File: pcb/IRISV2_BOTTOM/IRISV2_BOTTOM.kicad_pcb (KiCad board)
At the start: 4 copper layers, 50 x 50 mm, 92 parts, among them J1 Screw_Terminal_01x02, J10 Screw_Terminal_01x02, J11 Screw_Terminal_01x02, J12 Screw_Terminal_01x02, J13 Screw_Terminal_01x02, J14 Screw_Terminal_01x02, J15 Screw_Terminal_01x02, J16 Screw_Terminal_01x02, J3 Conn_01x20_MountingPin, J9 Screw_Terminal_01x02, Q1 BC846, Q10 PJA3404A, Q11 PJA3404A, Q12 PJA3404A, Q13 BC846, Q14 MCAC011P03L-TP, Q15 BC846, Q16 MCAC011P03L-TP, Q17 BC846, Q2 BC846, Q3 BC846, Q4 PJA3404A, Q5 PJA3404A, Q6 PJA3404A, Q7 BC846, Q8 BC846, Q9 BC846, U1 TPS613222ADBV, U2 INA237, U3 MP4323GDE-Z

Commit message: all main routing done, need to break out remaining gpio onto banks of mpu and ppu
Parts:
- added J4: Screw_Terminal_01x03, OSTTE030104:OSTTE030104, F.Cu at (165.7, 126.4)
- moved R43 2.23 mm to (166.8, 121.1), turned to -90 degrees
- moved Q9 1.65 mm to (170.4, 120.6)
- moved R46 1.63 mm to (167.8, 121.1)
- moved Q12 1.59 mm to (170.2, 116.8)
- moved R49 0.54 mm to (167.4, 119.6)
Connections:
- net buzzer renamed /buzzer
- net ina_scl renamed /ina_scl
- net ina_sda renamed /ina_sda
- J3 pad 13: GND -> /can_h
- J3 pad 15: GND -> /can_l
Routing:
- net /can_h: track 0.00 -> 61.6 mm, vias 0 -> 1
- net /can_l: track 0.00 -> 58.0 mm, vias 0 -> 1
- net c6_fire: track 50.8 -> 52.2 mm
- net /power_control/c6_-: track 5.80 -> 6.46 mm

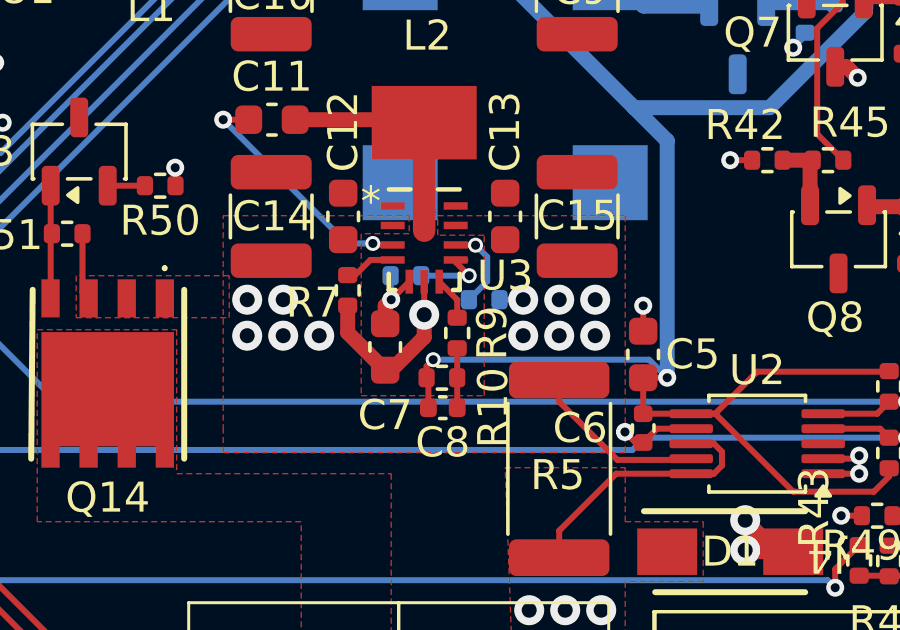
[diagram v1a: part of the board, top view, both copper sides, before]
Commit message: fixed some issues, lr2021 matching is now 0201 - todo change trace width to match pad width like ref design, see todo for rest
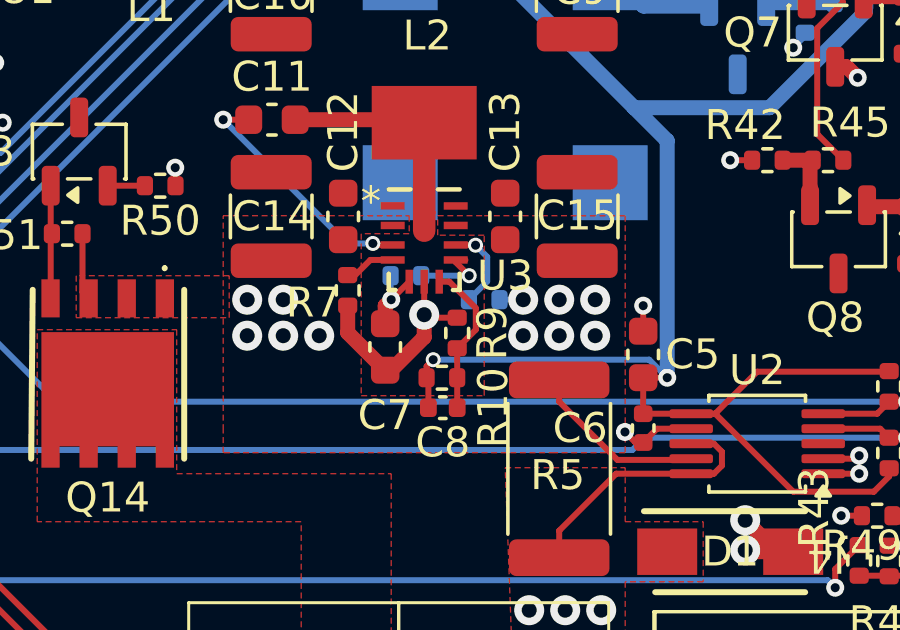
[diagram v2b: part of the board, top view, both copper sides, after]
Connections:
- C8 pad 1: Net-(C8-Pad1) -> /feedback
- R10 pad 2: Net-(C8-Pad1) -> /feedback
- R9 pad 1: /feedback -> GND
- R9 pad 2: Net-(C8-Pad1) -> /feedback
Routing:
- net /feedback: track 1.45 -> 5.16 mm
- net Net-(C8-Pad1): track 1.98 -> 0.00 mm
- net GND: track 20.3 -> 21.5 mm

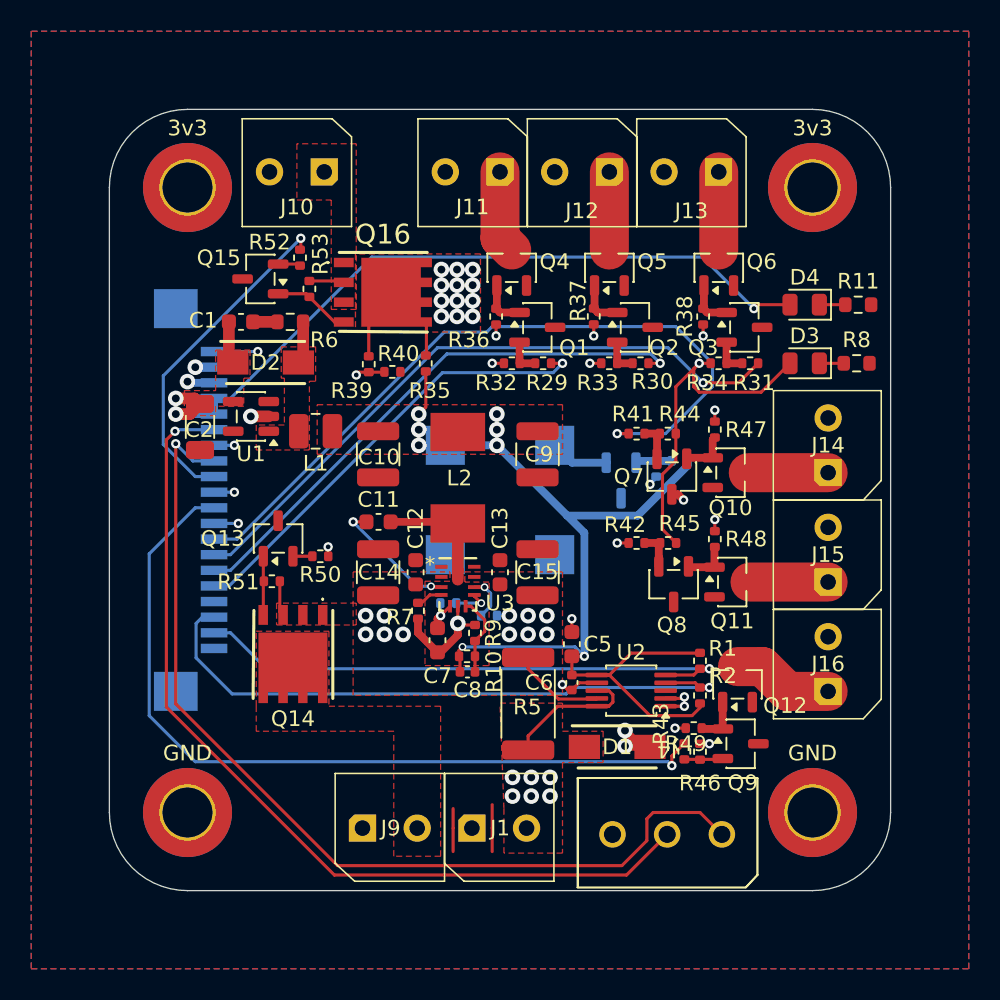
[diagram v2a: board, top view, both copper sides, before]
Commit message: removed usb, added connectors and stuff, 3d models mostly added, still need to route out gpio and servos (though connectors added)
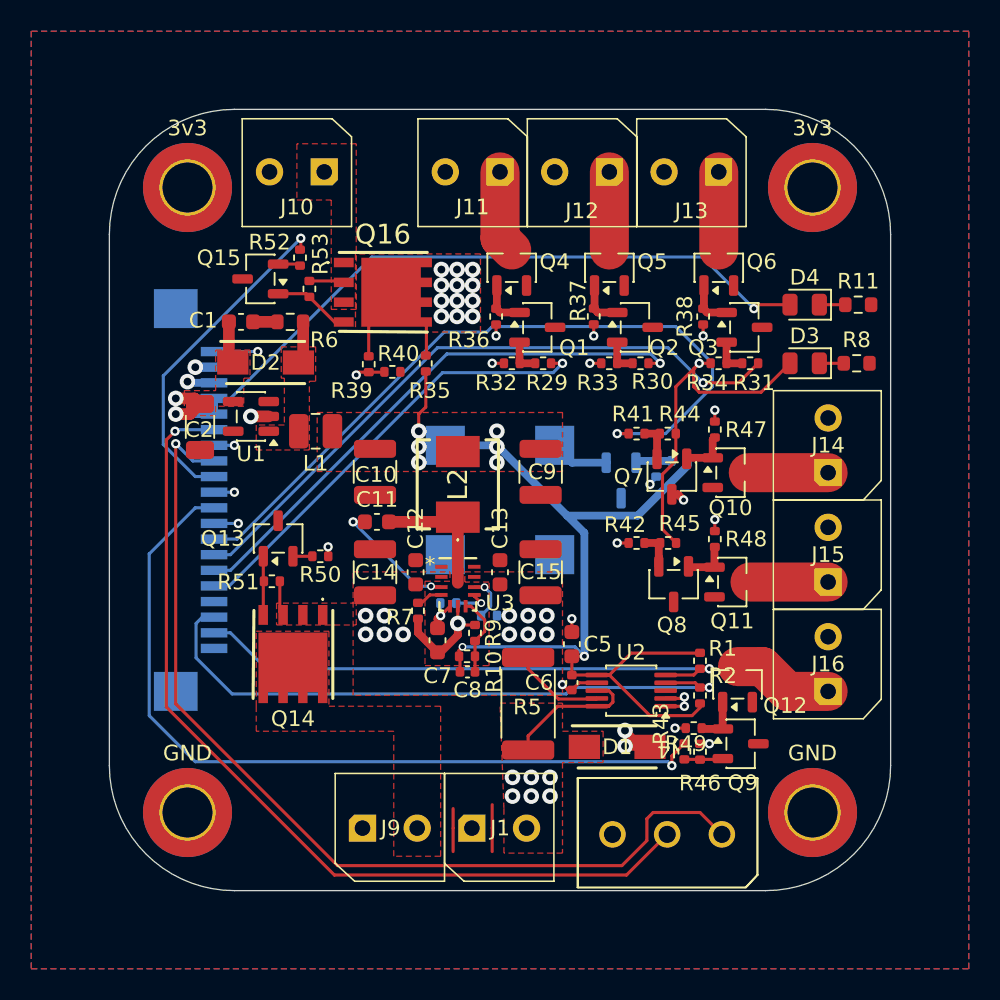
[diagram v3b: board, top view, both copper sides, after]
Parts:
- L2: footprint MGAH0603:MGAH0603 -> SPR5020TA-2R2M:SRP5020TA2R2M
- moved C10 1.14 mm to (147.0, 103.2)
- moved C9 1.14 mm to (157.6, 103.2)
- moved L2 0.42 mm to (152.3, 104.0)
- moved C14 0.20 mm to (147.0, 109.6)
- moved C15 0.20 mm to (157.6, 109.6)
- moved C11 0.10 mm to (147.1, 106.4)
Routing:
- net +3.3V: track 95.7 -> 96.8 mm
- net Net-(U3-SW): track 7.94 -> 8.72 mm
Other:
- outline, holes or cut-outs redrawn

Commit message: 3d models nearly done, just missing a few, gpio header routed - about to change lr2021 trace width
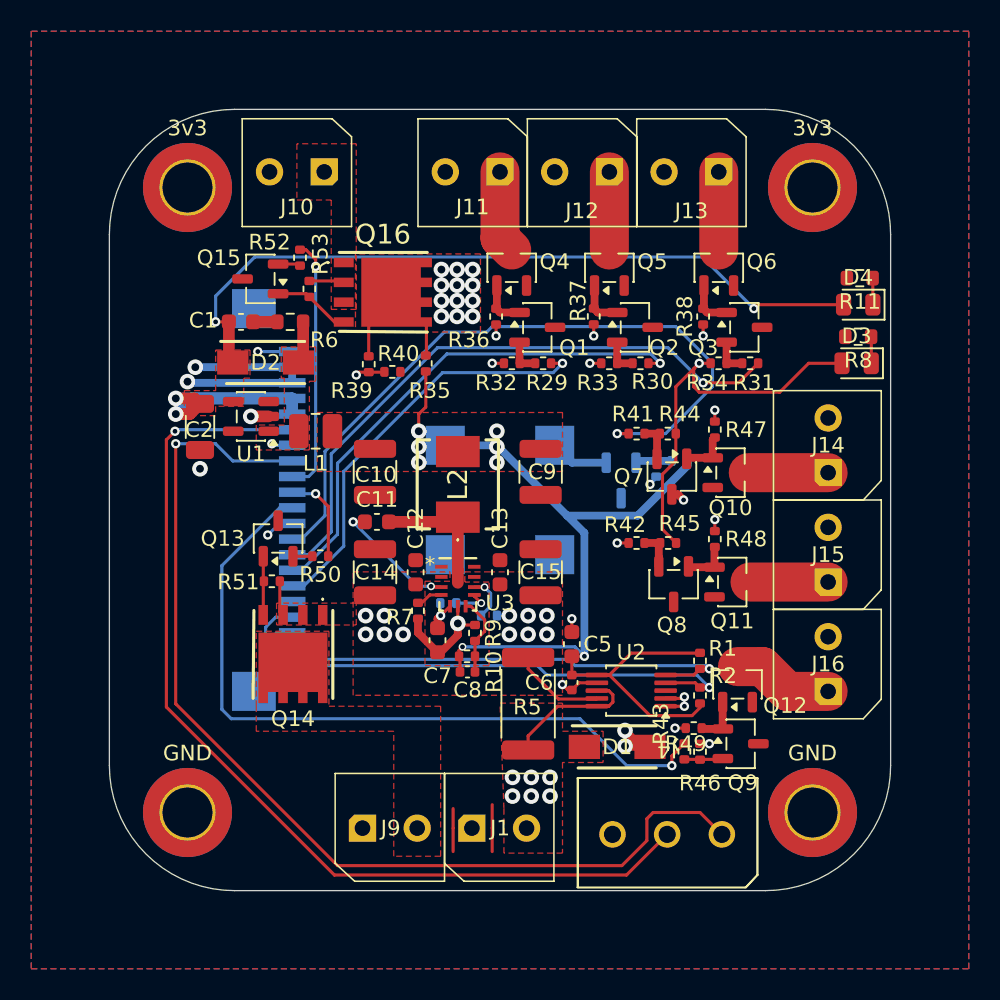
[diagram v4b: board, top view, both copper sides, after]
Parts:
- moved J3 5.00 mm to (141.7, 105.0)
- moved D4 3.43 mm to (177.9, 92.5)
- moved D3 3.32 mm to (177.8, 96.2)
- moved R8 1.70 mm to (177.9, 94.5), turned to 0 degrees
- moved R11 1.70 mm to (178.0, 90.8), turned to 0 degrees
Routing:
- net +5V: track 54.2 -> 67.7 mm, vias 3 -> 4
- net +5VP: track 51.6 -> 62.6 mm
- net arm: track 21.7 -> 16.4 mm
- net /can_l: track 58.0 -> 63.0 mm
- net /can_h: track 61.6 -> 66.6 mm
- net c6_fire: track 52.2 -> 47.3 mm
- net /ina_sda: track 40.4 -> 36.1 mm
- net c5_fire: track 31.7 -> 27.8 mm
- net camera_enable: track 9.35 -> 5.88 mm, vias 2 -> 1
- net +3.3V: track 96.8 -> 100.1 mm
- net c4_fire: track 48.1 -> 45.5 mm
- net cont_test: track 12.8 -> 10.4 mm
- net c2_fire: track 35.3 -> 33.0 mm
- net c1_fire: track 28.9 -> 26.7 mm
- net c3_fire: track 41.8 -> 39.7 mm
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
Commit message: pcb hopefully mostly finalized
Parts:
- added J2: Conn_01x02, Connector_PinHeader_2.54mm:PinHeader_1x02_P2.54mm_Vertical, F.Cu at (139.5, 128.2)
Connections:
- J3 pad 1: GND -> /cam_uart_tx
- J3 pad 4: GND -> /cam_uart_rx
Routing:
- net /cam_uart_rx: track 0.00 -> 20.6 mm, vias 0 -> 1
- net /cam_uart_tx: track 0.00 -> 18.4 mm, vias 0 -> 1
